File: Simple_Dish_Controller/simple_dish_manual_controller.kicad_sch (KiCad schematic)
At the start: 7 parts, among them J1 Screw_Terminal_01x02, SW1 SW_SPST, U1 AMS1117-5.0

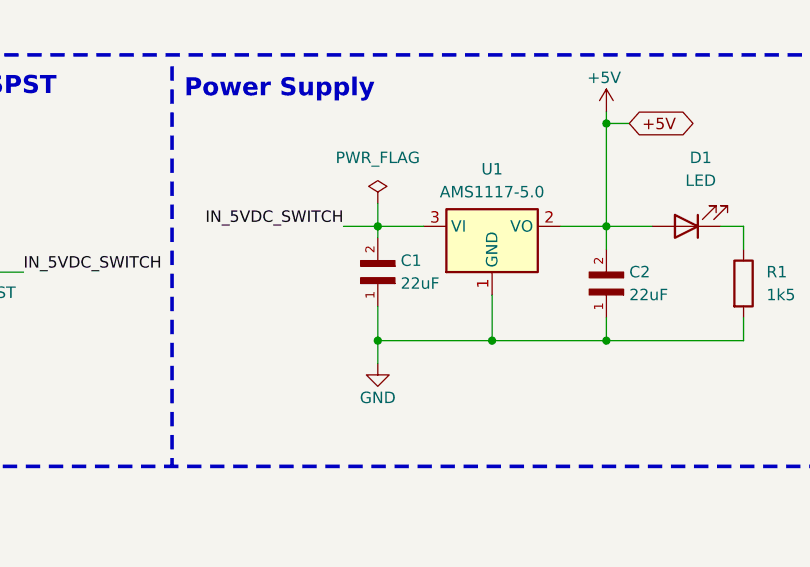
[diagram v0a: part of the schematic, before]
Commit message: Updated C1 cap part path
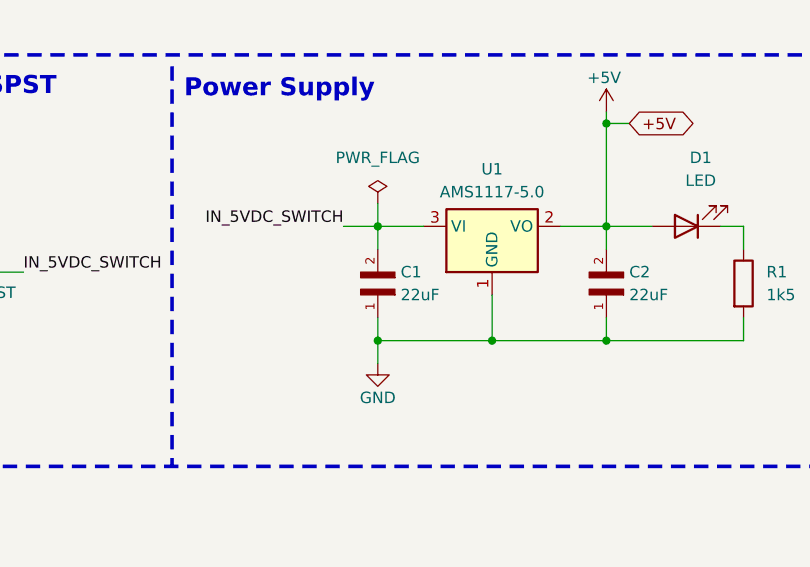
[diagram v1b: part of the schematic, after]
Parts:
- removed C1: 22uF, GRM219R61C226ME15K:CAPC2012X100N, symbol GRM219R61C226ME15K:GRM219R61C226ME15K
- added C1: 22uF, GRM219R61C226ME15K:CAPC2012X100N, symbol Cap_SMD_22uF_0805:GRM219R61C226ME15K
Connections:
- net GND: now also C1.1
- net IN_5VDC_SWITCH: now also C1.2
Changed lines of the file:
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@@
+	)
+	(junction
+		(at 181.61 110.49)
+		(diameter 0)
+		(color 0 0 0 0)
+	)
+	(junction
+		(at 168.91 110.49)
+		(diameter 0)
+		(color 0 0 0 0)
+	)
+	(junction
+		(at 181.61 86.36)
+		(diameter 0)
+		(color 0 0 0 0)
 	)
 	(junction
@@
 		(color 0 0 0 0)
 	)
-	(junction
-		(at 181.61 110.49)
-		(diameter 0)
-		(color 0 0 0 0)
-	)
-	(junction
-		(at 168.91 110.49)
-		(diameter 0)
-		(color 0 0 0 0)
-	)
-	(junction
-		(at 181.61 86.36)
-		(diameter 0)
-		(color 0 0 0 0)
-	)
 	(wire
 		(pts
@@
 		(pts
 			(xy 69.85 113.03) (xy 69.85 116.84)
-		)
-		(stroke
-			(width 0)
-			(type default)
-		)
-	)
-	(wire
-		(pts
-			(xy 156.21 97.79) (xy 156.21 99.06)
 		)
 		(stroke
@@
 	(wire
 		(pts
+			(xy 156.21 97.79) (xy 156.21 100.33)
+		)
+		(stroke
+			(width 0)
+			(type default)
+		)
+	)
+	(wire
+		(pts
 			(xy 81.28 114.3) (xy 81.28 118.11)
-		)
-		(stroke
-			(width 0)
-			(type default)
-		)
-	)
-	(wire
-		(pts
-			(xy 156.21 106.68) (xy 156.21 110.49)
 		)
 		(stroke
@@
 		(pts
 			(xy 181.61 97.79) (xy 181.61 100.33)
+		)
+		(stroke
+			(width 0)
+			(type default)
+		)
+	)
+	(wire
+		(pts
+			(xy 156.21 107.95) (xy 156.21 110.49)
 		)
 		(stroke
@@
 			"AAAAAAAAAAAAAAAAAAAAAAAAAAAAAAAAAAAAAAAAAAAAAAAAAAAAAAAAAAAAAAAAAAAAAAAAAAAA"
 			"AAAAAAAAAAAAAAAAAAAAAAAAAAAAAAAAAAAAAAAAAAAAAAAAAAAAAAAAAAAAAAAAAAAAAAAAAAAA"
+			"AAAAAAAAAAAAAAAAAAAAAAAAAAAAAAAAAAAAAAAAAAAAAAAAAAAAAAAAAAAAAAAAAAAAAAAAAAAA"
+			"AAAAAAAAAAAAAAAAAAAAAAAAAAAAAAAAAAAAAAAAAAAAAAAAAAAAAAAAAAAAAAAAAAAAAAAAAAAA"
+			"AAAAAAAAAAAAAAAAAAAAAAAAAAAAAAAAAAAAAAAAAAAAAAAAAAAAAAAAAAAAAAAAAAAAAAAAAAAA"
+			"AAAAAAAAAAAAAAAAAAAAAAAAAAAAAAAAAAAAAAAAAAAAAAAAAAAAAAAAAAAAAAAAAAAAAAAAAAAA"
+			"AAAAAAAAAAAAAAAAAAAAAAAAAAAAAAAAAAAAAAAAAAAAAAAAAAAAAAAAAAAAAAAAAAAAAAAAAAAA"
+			"AAAAAAAAAAAAAAAAAAAAAAAAAAAAAAAAAAAAAAAAAAAAAAAAAAAAAAAAAAAAAAAAAAAAAAAAAAAA"
+			"AAAAAAAAAAAAAAAAAAAAAAAAAAAAAAAAAAAAAAAAAAAAAAAAAAAAAAAAAAAAAAAAAAAAAAAAAAAA"
+			"AAAAAAAAAAAAAAAAAAAAAAAAAAAAAAAAAAAAAAAAAAAAAAAAAAAAAAAAAAAAAAAAAAAAAAAAAAAA"
+			"AAAAAAAAAAAAAAAAAAAAAAAAAAAAAAAAAAAAAAAAAAAAAAAAAAAAAAAAAAAAAAAAAAAAAAAAAAAA"
+			"AAAAAAAAAAAAAAAAAAAAAAAAAAAAAAAAAAAAAAAAAAAAAAAAAAAAAAAAAAAAAAAAAAAAAAAAAAAA"
+			"AAAAAAAAAAAAAAAAAAAAAAAAAAAAAAAAAAAAAAAAAAAAAAAAAAAAAAAAAAAAAAAAAAAAAAAAAAAA"
+			"AAAAAAAAAAAAAAAAAAAAAAAAAAAAAAAAAAAAAAAAAAAAAAAAAAAAAAAAAAAAAAAAAAAAAAAAAAAA"
+			"AAAAAAAAAAAAAAAAAAAAAAAAAAAAAAAAAAAAAAAAAAAAAAAAAAAAAAAAAAAAAAAAAAAAAAAAAAAA"
+			"AAAAAAAAAAAAAAAAAAAAAAAAAAAAAAAAAAAAAAAAAAAAAAAAAAAAAAAAAAAAAAAAAAAAAAAAAAAA"
+			"AAAAAAAAAAAAAAAAAAAAAAAAAAAAAAAAAAAAAAAAAAAAAAAAAAAAAAAAAAAAAAAAAAAAAAAAAAAA"
+			"AAAAAAAAAAAAAAAAAAAAAAAAAAAAAAAAAAAAAAAAAAAAAAAAAAAAAAAAAAAAAAAAAAAAAAAAAAAA"
+			"AAAAAAAAAAAAAAAAAAAAAAAAAAAAAAAAAAAAAAAAAAAAAAAAAAAAAAAAAAAAAAAAAAAAAAAAAAAA"
+			"AAAAAAAAAAAAAAAAAAAAAAAAAAAAAAAAAAAAAAAAAAAAAAAAAAAAAAAAAAAAAAAAAAAAAAAAAAAA"
+			"AAAAAAAAAAAAAAAAAAAAAAAAAAAAAAAAAAAAAAAAAAAAAAAAAAAAAAAAAAAAAAAAAAAAAAAAAAAA"
+			"AAAAAAAAAAAAAAAAAAAAAAAAAAAAAAAAAAAAAAAAAAAAAAAAAAAAAAAAAAAAAAAAAAAAAAAAAAAA"
+			"AAAAAAAAAAAAAAAAAAAAAAAAAAAAAAAAAAAAAAAAAAAAAAAAAAAAAAAAAAAAAAAAAAAAAAAAAAAA"
+			"AAAAAAAAAAAAAAAAAAAAAAAAAAAAAAAAAAAAAAAAAAAAAAAAAAAAAAAAAAAAAAAAAAAAAAAAAAAA"
+			"AAAAAAAAAAAAAAAAAAAAAAAAAAAAAAAAAAAAAAAAAAAAAAAAAAAAAAAAAAAAAAAAAAAAAAAAAAAA"
+			"AAAAAAAAAAAAAAAAAAAAAAAAAAAAAAAAAAAAAAAAAAAAAAAAAAAAAAAAAAAAAAAAAAAAAAAAAAAA"
+			"AAAAAAAAAAAAAAAAAAAAAAAAAAAAAAAAAAAAAAAAAAAAAAAAAAAAAAAAAAAAAAAAAAAAAAAAAAAA"
+			"AAAAAAAAAAAAAAAAAAAAAAAAAAAAAAAAAAAAAAAAAAAAAAAAAAAAAAAAAAAAAAAAAAAAAAAAAAAA"
+			"AAAAAAAAAAAAAAAAAAAAAAAAAAAAAAAAAAAAAAAAAAAAAAAAAAAAAAAAAAAAAAAAAAAAAAAAAAAA"
+			"AAAAAAAAAAAAAAAAAAAAAAAAAAAAAAAAAAAAAAAAAAAAAAAAAAAAAAAAAAAAAAAAAAAAAAAAAAAA"
+			"AAAAAAAAAAAAAAAAAAAAAAAAAAAAAAAAAAAAAAAAAAAAAAAAAAAAAAAAAAAAAAAAAAAAAAAAAAAA"
+			"AAAAAAAAAAAAAAAAAAAAAAAAAAAAAAAAAAAAAAAAAAAAAAAAAAAAAAAAAAAAAAAAAAAAAAAAAAAA"
+			"AAAAAAAAAAAAAAAAAAAAAAAAAAAAAAAAAAAAAAAAAAAAAAAAAAAAAAAAAAAAAAAAAAAAAAAAAAAA"
+			"AAAAAAAAAAAAAAAAAAAAAAAAAAAAAAAAAAAAAAAAAAAAAAAAAAAAAAAAAAAAAAAAAAAAAAAAAAAA"
+			"AAAAAAAAAAAAAAAAAAAAAAAAAAAAAAAAAAAAAAAAAAAAAAAAAAAAAAAAAAAAAAAAAAAAAAAAAAAA"
+			"AAAAAAAAAAAAAAAAAAAAAAAAAAAAAAAAAAAAAAAAAAAAAAAAAAAAAAAAAAAAAAAAAAAAAAAAAAAA"
+			"AAAAAAAAAAAAAAAAAAAAAAAAAAAAAAAAAAAAAAAAAAAAAAAAAAAAAAAAAAAAAAAAAAAAAAAAAAAA"
+			"AAAAAAAAAAAAAAAAAAAAAAAAAAAAAAAAAAAAAAAAAAAAAAAAAAAAAAAAAAAAAAAAAAAAAAAAAAAA"
 			"AAAAAAAAAAAAAAAAAAAAAAAAAAAAAAAAAAAAAA=="
 		)
@@
 	)
 	(symbol
-		(lib_id "GRM219R61C226ME15K:GRM219R61C226ME15K")
-		(at 156.21 104.14 90)
-		(unit 1)
-		(exclude_from_sim no)
-		(in_bom yes)
-		(on_board yes)
-		(dnp no)
-		(property "Reference" "C1"
-			(at 158.75 101.6 90)
-			(effects
-				(font
-					(size 1.27 1.27)
-				)
-				(justify right)
-			)
-		)
-		(property "Value" "22uF"
-			(at 158.75 104.14 90)
-			(effects
-				(font
-					(size 1.27 1.27)
-				)
-				(justify right)
-			)
-		)
-		(property "Footprint" "GRM219R61C226ME15K:CAPC2012X100N"
-			(at 156.21 104.14 0)
-			(effects
-				(font
-					(size 1.27 1.27)
-				)
-				(justify bottom)
-				(hide yes)
-			)
-		)
-		(property "Datasheet" ""
-			(at 156.21 104.14 0)
-			(effects
-				(font
-					(size 1.27 1.27)
-				)
-				(hide yes)
-			)
-		)
-		(property "Description" ""
-			(at 156.21 104.14 0)
-			(effects
-				(font
-					(size 1.27 1.27)
-				)
-				(hide yes)
-			)
-		)
-		(property "MF" "Murata"
-			(at 156.21 104.14 0)
-			(effects
-				(font
-					(size 1.27 1.27)
-				)
-				(justify bottom)
-				(hide yes)
-			)
-		)
-		(property "Description_1" "SMD Capacitor X5R(EIA) with Capacitance: 22uF Tol. 20%. Rated Voltage: 16Vdc"
-			(at 156.21 104.14 0)
-			(effects
-				(font
-					(size 1.27 1.27)
-				)
-				(justify bottom)
-				(hide yes)
-			)
-		)
-		(property "Package" "805-2 Murata"
-			(at 156.21 104.14 0)
-			(effects
-				(font
-					(size 1.27 1.27)
-				)
-				(justify bottom)
-				(hide yes)
-			)
-		)
-		(property "Price" "None"
-			(at 156.21 104.14 0)
-			(effects
-				(font
-					(size 1.27 1.27)
-				)
-				(justify bottom)
-				(hide yes)
-			)
-		)
-		(property "SnapEDA_Link" "https://www.snapeda.com/parts/GRM219R61C226ME15K/Murata/view-part/?ref=snap"
-			(at 156.21 104.14 0)
-			(effects
-				(font
-					(size 1.27 1.27)
-				)
-				(justify bottom)
-				(hide yes)
-			)
-		)
-		(property "MP" "GRM219R61C226ME15K"
-			(at 156.21 104.14 0)
-			(effects
-				(font
-					(size 1.27 1.27)
-				)
-				(justify bottom)
-				(hide yes)
-			)
-		)
-		(property "Availability" "In Stock"
-			(at 156.21 104.14 0)
-			(effects
-				(font
-					(size 1.27 1.27)
-				)
-				(justify bottom)
-				(hide yes)
-			)
-		)
-		(property "Check_prices" "https://www.snapeda.com/parts/GRM219R61C226ME15K/Murata/view-part/?ref=eda"
-			(at 156.21 104.14 0)
-			(effects
-				(font
-					(size 1.27 1.27)
-				)
-				(justify bottom)
-				(hide yes)
-			)
-		)
-		(pin "2"
-		)
-		(pin "1"
-		)
-		(instances
-			(project ""
-				(path "/8648ccd3-30ce-4b98-baff-aeab56a7c9f5"
-					(reference "C1")
-					(unit 1)
-				)
-			)
-		)
-	)
-	(symbol
 		(lib_id "power:PWR_FLAG")
 		(at 156.21 95.25 0)
@@
 					(unit 1)
 				)
+			)
+		)
+	)
+	(symbol
+		(lib_id "Cap_SMD_22uF_0805:GRM219R61C226ME15K")
+		(at 156.21 105.41 90)
+		(unit 1)
+		(exclude_from_sim no)
+		(in_bom yes)
+		(on_board yes)
+		(dnp no)
+		(property "Reference" "C1"
+			(at 158.75 102.87 90)
+			(effects
+				(font
+					(size 1.27 1.27)
+				)
+				(justify right)
+			)
+		)
+		(property "Value" "22uF"
+			(at 158.75 105.41 90)
+			(effects
+				(font
+					(size 1.27 1.27)
+				)
+				(justify right)
+			)
+		)
+		(property "Footprint" "GRM219R61C226ME15K:CAPC2012X100N"
+			(at 156.21 105.41 0)
+			(effects
+				(font
+					(size 1.27 1.27)
+				)
+				(justify bottom)
+				(hide yes)
+			)
+		)
+		(property "Datasheet" ""
+			(at 156.21 105.41 0)
+			(effects
+				(font
+					(size 1.27 1.27)
+				)
+				(hide yes)
+			)
+		)
+		(property "Description" ""
+			(at 156.21 105.41 0)
+			(effects
+				(font
+					(size 1.27 1.27)
+				)
+				(hide yes)
+			)
+		)
+		(property "MF" "Murata"
+			(at 156.21 105.41 0)
+			(effects
+				(font
+					(size 1.27 1.27)
+				)
+				(justify bottom)
+				(hide yes)
+			)
+		)
+		(property "Description_1" "SMD Capacitor X5R(EIA) with Capacitance: 22uF Tol. 20%. Rated Voltage: 16Vdc"
+			(at 156.21 105.41 0)
+			(effects
+				(font
+					(size 1.27 1.27)
+				)
+				(justify bottom)
+				(hide yes)
+			)
+		)
+		(property "Package" "805-2 Murata"
+			(at 156.21 105.41 0)
+			(effects
+				(font
+					(size 1.27 1.27)
+				)
+				(justify bottom)
+				(hide yes)
+			)
+		)
+		(property "Price" "None"
+			(at 156.21 105.41 0)
+			(effects
+				(font
+					(size 1.27 1.27)
+				)
+				(justify bottom)
+				(hide yes)
+			)
+		)
+		(property "SnapEDA_Link" "https://www.snapeda.com/parts/GRM219R61C226ME15K/Murata/view-part/?ref=snap"
+			(at 156.21 105.41 0)
+			(effects
+				(font
+					(size 1.27 1.27)
+				)
+				(justify bottom)
+				(hide yes)
+			)
+		)
+		(property "MP" "GRM219R61C226ME15K"
+			(at 156.21 105.41 0)
+			(effects
+				(font
+					(size 1.27 1.27)
+				)
+				(justify bottom)
+				(hide yes)
+			)
+		)
+		(property "Availability" "In Stock"
+			(at 156.21 105.41 0)
+			(effects
+				(font
+					(size 1.27 1.27)
+				)
+				(justify bottom)
+				(hide yes)
+			)
+		)
+		(property "Check_prices" "https://www.snapeda.com/parts/GRM219R61C226ME15K/Murata/view-part/?ref=eda"
+			(at 156.21 105.41 0)
+			(effects
+				(font
+					(size 1.27 1.27)
+				)
+				(justify bottom)
+				(hide yes)
+			)
+		)
+		(pin "2"
+		)
+		(pin "1"
+		)
+		(instances
+			(project ""
+				(path "/8648ccd3-30ce-4b98-baff-aeab56a7c9f5"
+					(reference "C1")
+					(unit 1)
+				)

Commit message: Added RJ45 ports
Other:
- note added: "Power Input and Conditioning - 5V"
- moved on the sheet: C1, C2, D1, J1, R1, SW1, U1
